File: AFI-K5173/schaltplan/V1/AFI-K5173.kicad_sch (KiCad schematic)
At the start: 42 parts, among them J1 KES BUS, J2 IDE Chan A, J3 Front Panel, U1 74HCT573, U10 74HCT04, U11 74HCT04, U12 74HCT04, U13 74AHCT04, U14 74HCT32, U15 74HCT138, U16 74HCT08, U17 74HCT20, U18 74HCT20, U19 74HCT74, U2 74HCT573, U20 74HCT138, U3 74HCT573, U4 74HCT573, U5 74HCT573, U6 74HCT573, U7 74HCT640, U8 74HCT573, U9 SST39SF040

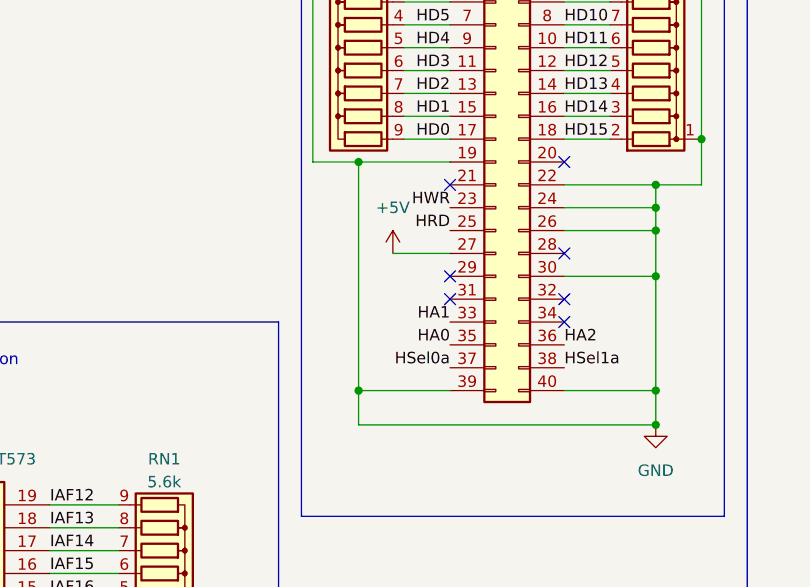
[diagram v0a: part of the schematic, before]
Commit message: Bigfix Schaltung/PCB: Pin 39 des IDE-Steckers darf nicht auf Masse liegen. Das verursacht eine exrem lange Bootphase bei bestimmten Platten-Konfigurationen.
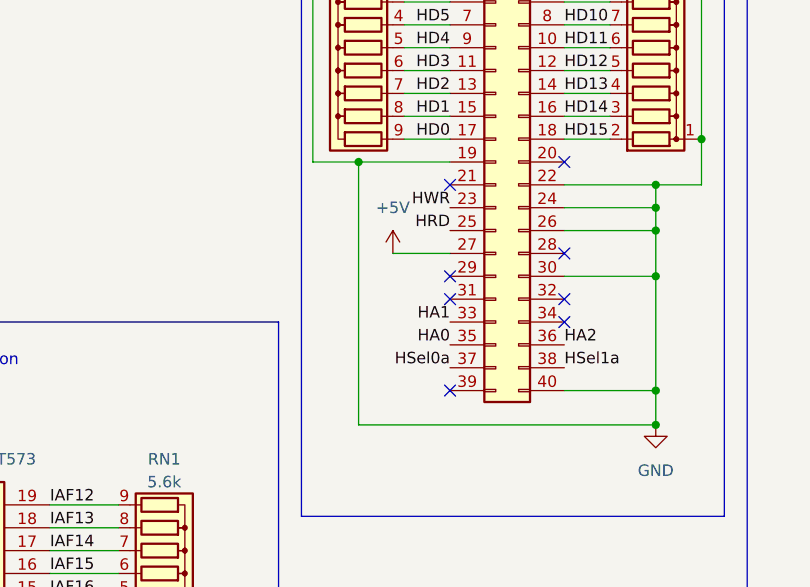
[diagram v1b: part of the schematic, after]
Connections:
- net GND: no longer J2.39 (Pin_39)
- no-connect marks 69 -> 70
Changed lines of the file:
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@@
     (title "AFI-K5173 IDE-Controller for A7150 (CM1910)")
     (date "27.08.2022")
-    (rev "1.0a")
+    (rev "1.1")
     (company "Autor: Stefan Berndt")
+    (comment 1 "Rev 1.1: J2 (IDE) Pin 39 (DASP) darf nicht auf Masse liegen.")
   )
   (junction (at 85.09 170.18) (diameter 0) (color 0 0 0 0)
@@
   )
   (junction (at 323.85 63.5) (diameter 0) (color 0 0 0 0)
-  )
-  (junction (at 290.83 76.2) (diameter 0) (color 0 0 0 0)
   )
   (junction (at 69.85 261.62) (diameter 0) (color 0 0 0 0)
@@
   (no_connect (at 53.34 215.9))
   (no_connect (at 53.34 213.36))
+  (no_connect (at 300.99 76.2))
   (no_connect (at 313.69 68.58))
   (no_connect (at 313.69 66.04))
@@
     (stroke (width 0) (type default) (color 0 0 0 0))
   )
-  (wire (pts (xy 290.83 76.2) (xy 290.83 50.8))
-    (stroke (width 0) (type default) (color 0 0 0 0))
-  )
   (wire (pts (xy 17.78 149.86) (xy 58.42 149.86))
     (stroke (width 0) (type default) (color 0 0 0 0))
@@
   )
   (polyline (pts (xy 82.55 182.88) (xy 82.55 129.54))
-    (stroke (width 0) (type default) (color 0 0 0 0))
-  )
-  (wire (pts (xy 290.83 76.2) (xy 300.99 76.2))
     (stroke (width 0) (type default) (color 0 0 0 0))
   )
@@
     (stroke (width 0) (type default) (color 0 0 0 0))
   )
-  (wire (pts (xy 290.83 80.01) (xy 290.83 76.2))
-    (stroke (width 0) (type default) (color 0 0 0 0))
-  )
+  (wire (pts (xy 290.83 50.8) (xy 290.83 80.01))
+    (stroke (width 0) (type default) (color 0 0 0 0))
+  )

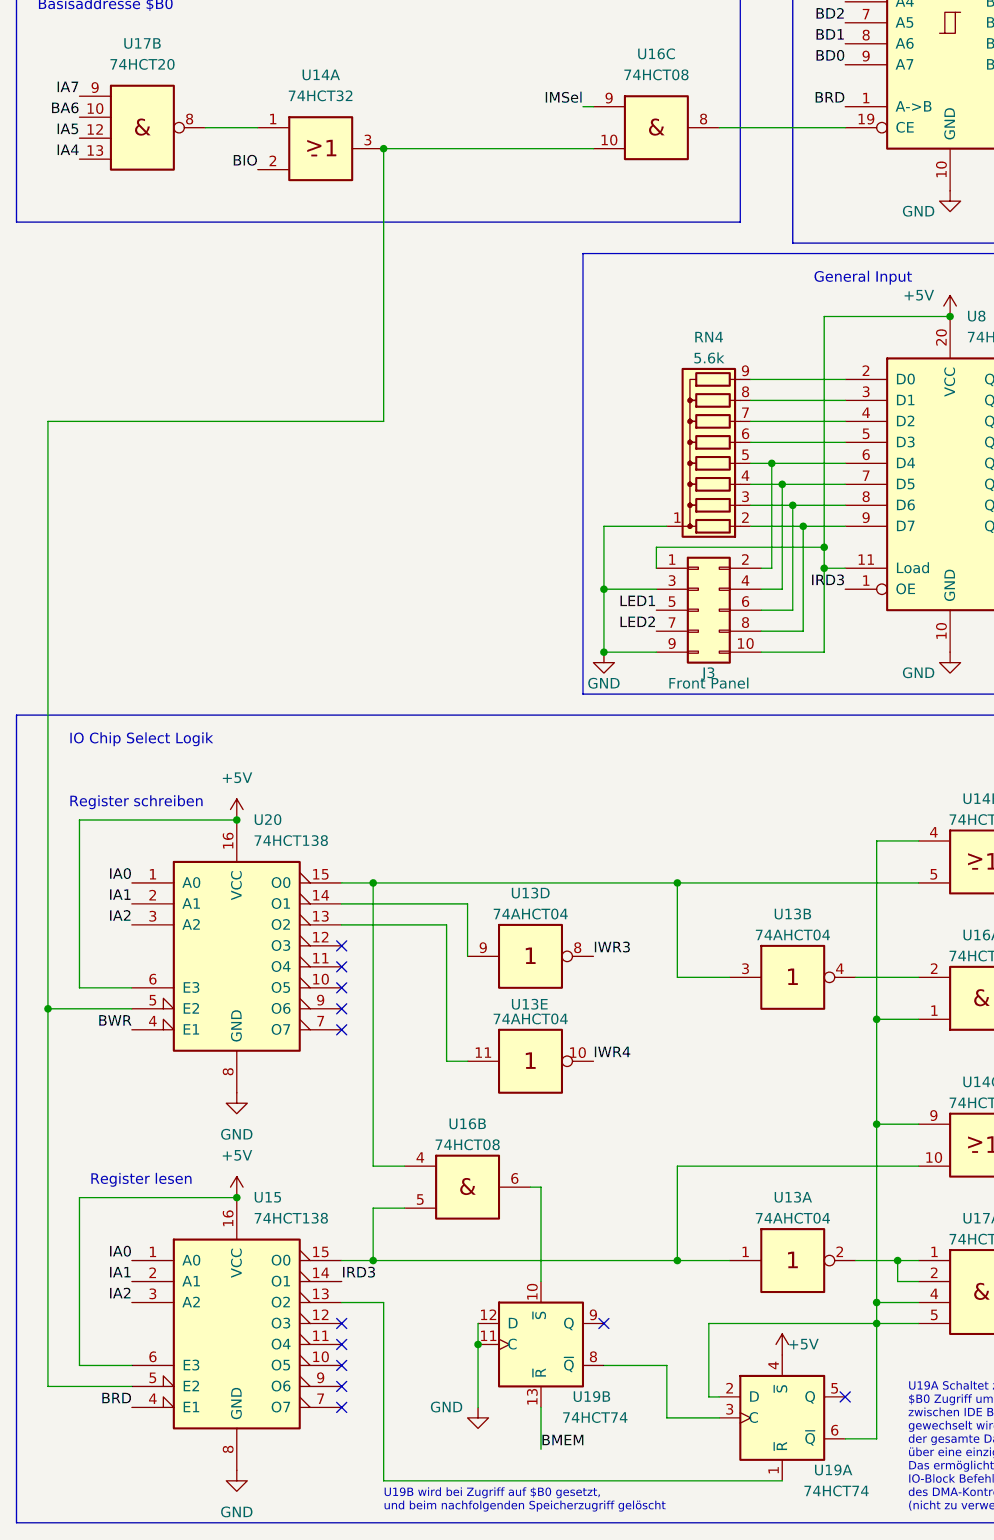
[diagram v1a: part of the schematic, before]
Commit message: Schaltung/PCB: Anschluss für USB-Kontroller-Platine hinzugefügt
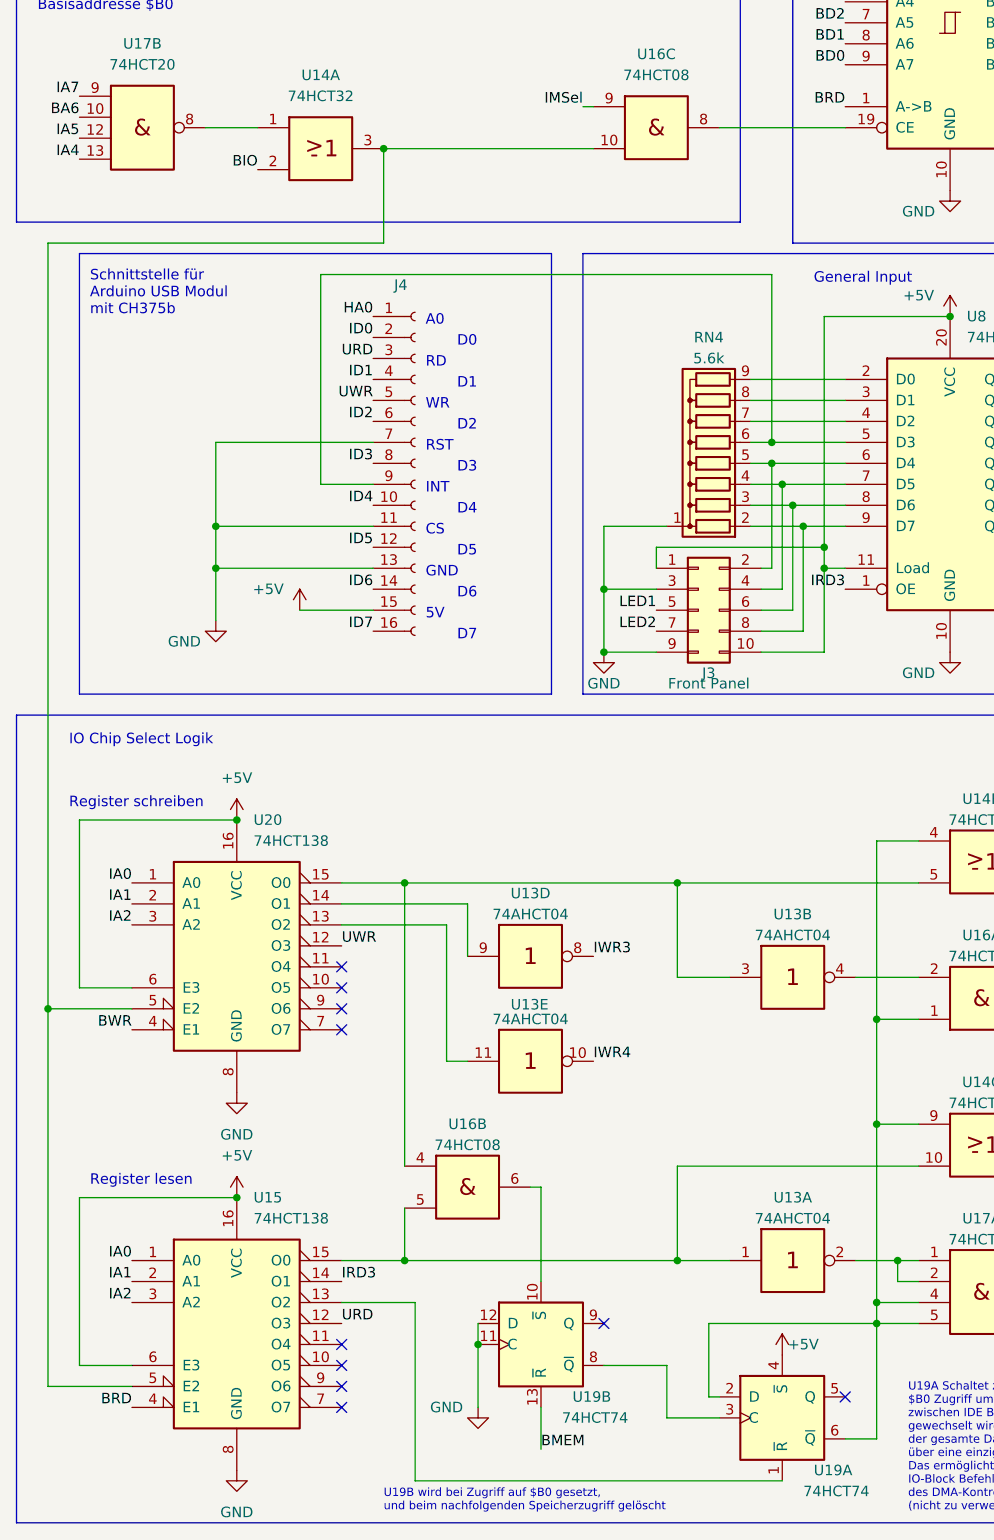
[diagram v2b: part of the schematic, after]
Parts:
- added J4: Conn_01x16_Female, Connector_PinSocket_2.54mm:PinSocket_2x08_P2.54mm_Vertical, symbol Connector:Conn_01x16_Female
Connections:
- net +5V: now also J4.15 (Pin_15)
- net GND: now also J4.11 (Pin_11), J4.13 (Pin_13), J4.7 (Pin_7)
- net HA0: now also J4.1 (Pin_1)
- net ID0: now also J4.2 (Pin_2)
- net ID1: now also J4.4 (Pin_4)
- net ID2: now also J4.6 (Pin_6)
- net ID3: now also J4.8 (Pin_8)
- net ID4: now also J4.10 (Pin_10)
- net ID5: now also J4.12 (Pin_12)
- net ID6: now also J4.14 (Pin_14)
- net ID7: now also J4.16 (Pin_16)
- net UWR: now reaches U20.12 (O3)
- net UWR: now also J4.5 (Pin_5)
- net URD: now reaches U15.12 (O3)
- net URD: now also J4.3 (Pin_3)
- net at RN4.6 (R5), U8.5 (D3): now also J4.9 (Pin_9)
- no-connect marks 70 -> 68
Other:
- note added: "5V"
- note added: "A0"
- note added: "CS"
- note added: "D0"
- note added: "D1"
- note added: "D2"
- note added: "D3"
- note added: "D4"
- note added: "D5"
- note added: "D6"
- note added: "D7"
- note added: "GND"
- note added: "INT"
- note added: "RD"
- note added: "RST"
- note added: "Schnittstelle für Arduino USB Modul mit CH375b"
- note added: "WR"

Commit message: Schaltungsänderung und Layout V0.3
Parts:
- added R3, R4: 39, Resistor_THT:R_Axial_DIN0309_L9.0mm_D3.2mm_P2.54mm_Vertical, symbol Device:R
- added R5: 220, Resistor_THT:R_Axial_DIN0309_L9.0mm_D3.2mm_P2.54mm_Vertical, symbol Device:R
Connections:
- net +5V: now also R5.1; no longer J3.1 (Pin_1), J3.10 (Pin_10)
- net HRD: now also R4.1; no longer J2.25 (Pin_25)
- net HWR: now also R3.1; no longer J2.23 (Pin_23)
- new net: J2.23 (Pin_23), R3.2
- new net: J2.25 (Pin_25), R4.2
- new net: J3.1 (Pin_1), J3.10 (Pin_10), R5.2
